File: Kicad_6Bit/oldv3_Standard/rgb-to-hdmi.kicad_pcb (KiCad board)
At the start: 2 copper layers, 67.6 x 30.5 mm, 42 parts, among them J2 Conn_02x01, P1 CONN_02X20, P2 Conn_02x05_Odd_Even, P3 Conn_01x06, P4 CONN_01X02, P5 Conn_01x04, SW1 SW_PUSH, SW2 SW_PUSH, SW3 SW_PUSH, SW4 SW_PUSH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

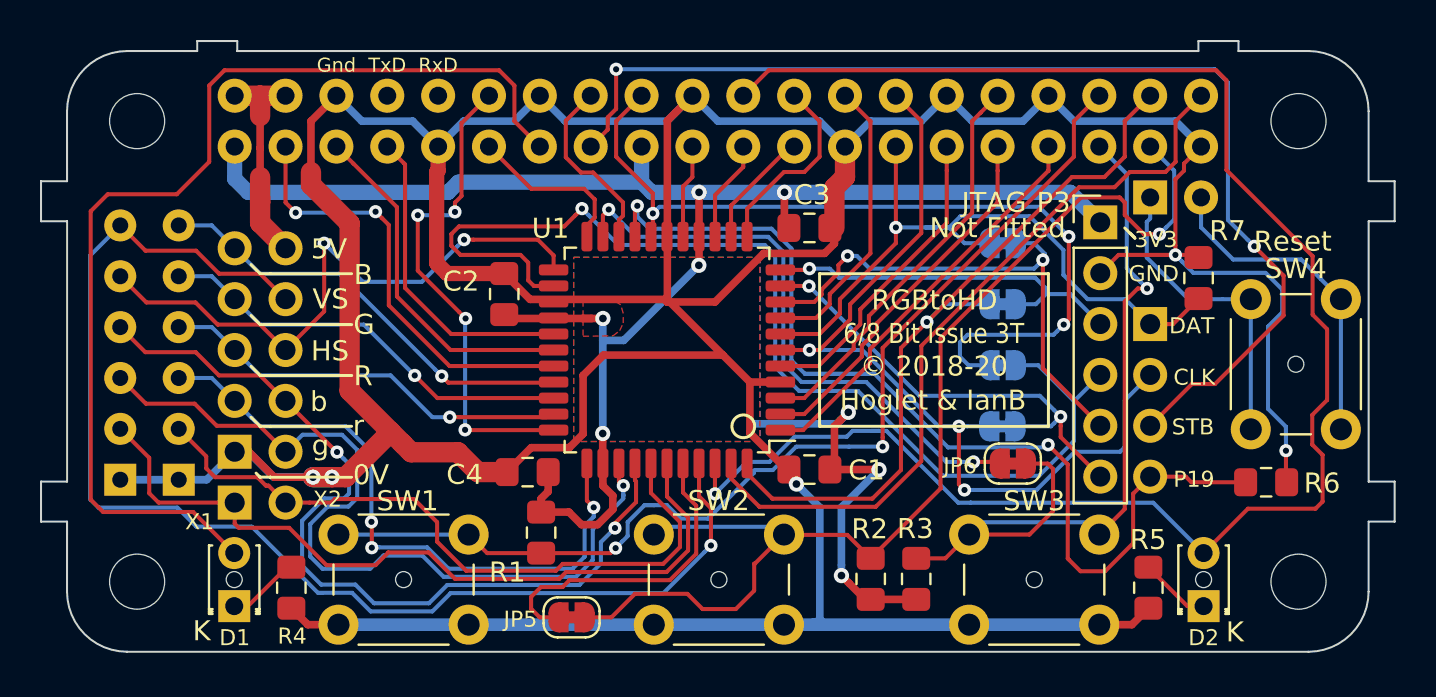
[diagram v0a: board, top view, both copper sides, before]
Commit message: Update 6/8 bit boards with identity resistor
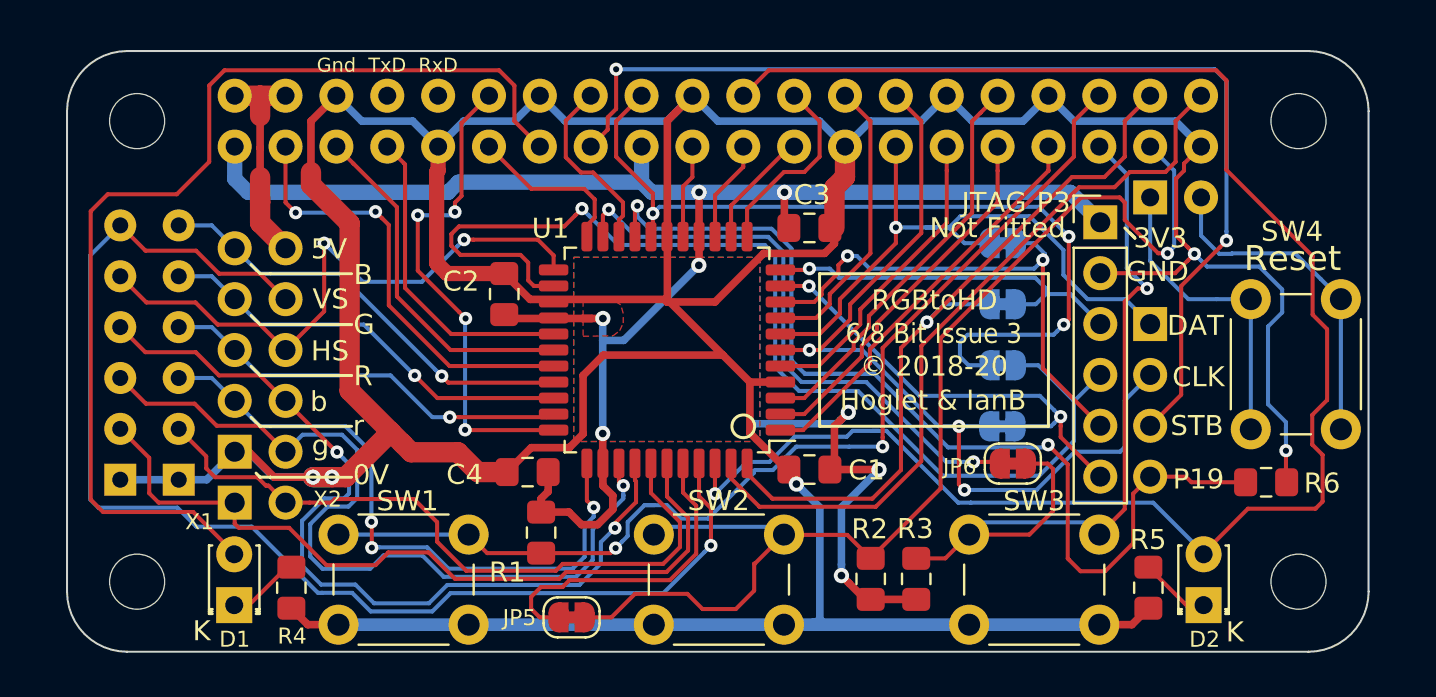
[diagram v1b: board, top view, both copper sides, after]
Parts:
- removed  : mountinghole_1mm, MountingHole:mountinghole_1mm (x6)
- removed R7: 1K, Resistor_SMD:R_0805_2012Metric_Pad1.15x1.40mm_HandSolder
- D1, D2: footprint LED_THT:LED_D1.8mm_W3.3mm_H2.4mm_Custom -> LED_THT:LED_D1.8mm_W3.3mm_H2.4mm
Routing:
- net /GPIO0: track 35.5 -> 32.3 mm
- net /GPIO22: track 57.5 -> 54.4 mm
- net /GPIO26: track 57.5 -> 59.3 mm
- net /GND: track 251.6 -> 250.9 mm
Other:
- board size 67.6 x 30.5 mm -> 65 x 30 mm
- board text added: "6/8 Bit Issue 3"
- board text removed: "6/8 Bit Issue 3T"
